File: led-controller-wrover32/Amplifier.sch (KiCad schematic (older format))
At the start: 5 parts, among them J11 Conn_01x02, U5 MAX98357A

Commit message: Cleanup
Signed-off-by: Aaron Williams <aaron.w2@gmail.com>
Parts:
- added J10: Conn_01x02 DNS, Connector_PinHeader_1.27mm:PinHeader_1x02_P1.27mm_Vertical_SMD_Pin1Left, symbol Connector_Generic:Conn_01x02
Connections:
- net SPKR+: now also J10.1 (Pin_1)
- net SPKR-: now also J10.2 (Pin_2)
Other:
- moved on the sheet: J11
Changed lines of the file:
@@
 EESchema Schematic File Version 4
-LIBS:led-controller-wrover32-cache
 EELAYER 30 0
 EELAYER END
 $Descr A4 11693 8268
 encoding utf-8
-Sheet 3 4
+Sheet 3 5
 Title ""
 Date ""
@@
 	1    0    0    -1
 $EndComp
-$Comp
-L Connector_Generic:Conn_01x02 J11
-U 1 1 5DBCE011
-P 5100 3200
-F 0 "J11" H 5180 3192 50  0000 L CNN
-F 1 "Conn_01x02" H 5180 3101 50  0000 L CNN
-F 2 "Aaron:JST_SH_BM02B-SRSS-TB_1x02-1MP_P1.00mm_Vertical" H 5100 3200 50  0001 C CNN
-F 3 "https://media.digikey.com/pdf/Data%20Sheets/JST%20PDFs/SR%20Connector.pdf" H 5100 3200 50  0001 C CNN
-F 4 "JST Sales America Inc." H 5100 3200 50  0001 C CNN "MFR"
-F 5 "BM02B-SRSS-TB(LF)(SN)" H 5100 3200 50  0001 C CNN "MPN"
-F 6 "Digikey" H 5100 3200 50  0001 C CNN "SPR"
-F 7 "455-1788-1-ND" H 5100 3200 50  0001 C CNN "SPN"
-F 8 "https://www.digikey.com/product-detail/en/jst-sales-america-inc/BM02B-SRSS-TB-LF-SN/455-1788-1-ND/926859" H 5100 3200 50  0001 C CNN "SPURL"
-	1    5100 3200
-	1    0    0    -1
-$EndComp
 Wire Wire Line
 	3200 3100 2650 3100
@@
 SPKR-
 Wire Wire Line
+	4550 3100 4900 3100
+Wire Wire Line
 	4900 3100 4900 3200
-Wire Wire Line
-	4550 3100 4900 3100
-Wire Wire Line
-	4550 3300 4900 3300
+$Comp
+L Connector_Generic:Conn_01x02 J11
+U 1 1 5DBCE011
+P 5200 3200
+F 0 "J11" H 5280 3192 50  0000 L CNN
+F 1 "Conn_01x02" H 5280 3101 50  0000 L CNN
+F 2 "Aaron:JST_SH_BM02B-SRSS-TB_1x02-1MP_P1.00mm_Vertical" H 5200 3200 50  0001 C CNN
+F 3 "https://media.digikey.com/pdf/Data%20Sheets/JST%20PDFs/SR%20Connector.pdf" H 5200 3200 50  0001 C CNN
+F 4 "JST Sales America Inc." H 5200 3200 50  0001 C CNN "MFR"
+F 5 "BM02B-SRSS-TB(LF)(SN)" H 5200 3200 50  0001 C CNN "MPN"
+F 6 "Digikey" H 5200 3200 50  0001 C CNN "SPR"
+F 7 "455-1788-1-ND" H 5200 3200 50  0001 C CNN "SPN"
+F 8 "https://www.digikey.com/product-detail/en/jst-sales-america-inc/BM02B-SRSS-TB-LF-SN/455-1788-1-ND/926859" H 5200 3200 50  0001 C CNN "SPURL"
+	1    5200 3200
+	1    0    0    -1
+$EndComp
+$Comp
+L Connector_Generic:Conn_01x02 J10
+U 1 1 5E133F76
+P 5200 3600
+F 0 "J10" H 5280 3592 50  0000 L CNN
+F 1 "Conn_01x02 DNS" H 5280 3501 50  0000 L CNN
+F 2 "Connector_PinHeader_1.27mm:PinHeader_1x02_P1.27mm_Vertical_SMD_Pin1Left" H 5200 3600 50  0001 C CNN
+F 3 "https://media.digikey.com/pdf/Data%20Sheets/JST%20PDFs/SR%20Connector.pdf" H 5200 3600 50  0001 C CNN
+F 4 "JST Sales America Inc." H 5200 3600 50  0001 C CNN "MFR"
+F 5 "BM02B-SRSS-TB(LF)(SN)" H 5200 3600 50  0001 C CNN "MPN"
+F 6 "Digikey" H 5200 3600 50  0001 C CNN "SPR"
+F 7 "455-1788-1-ND" H 5200 3600 50  0001 C CNN "SPN"
+F 8 "https://www.digikey.com/product-detail/en/jst-sales-america-inc/BM02B-SRSS-TB-LF-SN/455-1788-1-ND/926859" H 5200 3600 50  0001 C CNN "SPURL"
+	1    5200 3600
+	1    0    0    -1
+$EndComp
+Wire Wire Line
+	4900 3200 5000 3200
+Wire Wire Line
+	4550 3300 4800 3300
+Wire Wire Line
+	4900 3200 4900 3600
+Wire Wire Line
+	4900 3600 5000 3600
+Connection ~ 4900 3200
+Wire Wire Line
+	4800 3300 4800 3700
+Wire Wire Line
+	4800 3700 5000 3700
+Connection ~ 4800 3300
+Wire Wire Line
+	4800 3300 5000 3300
 $EndSCHEMATC

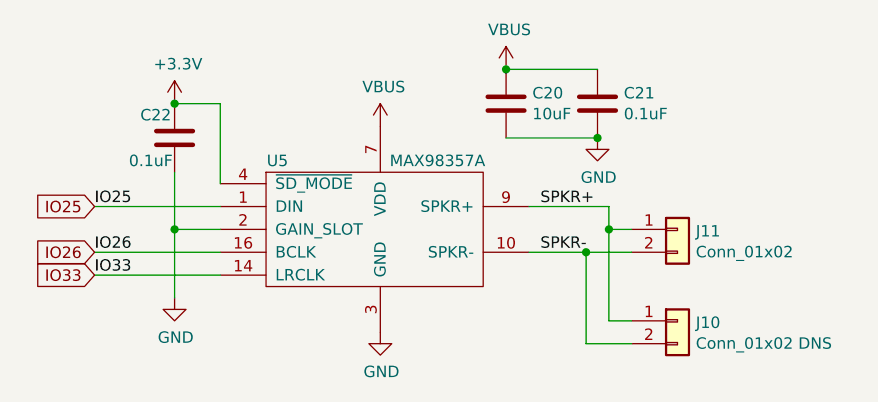
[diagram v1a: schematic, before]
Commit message: Fix reset circuit and other stuff
This fixes the reset circuit and moves a few components.  It also
cleans up the BOM a bit.

Also bumped to version 3.5.0

Signed-off-by: Aaron Williams <aaron.w2@gmail.com>
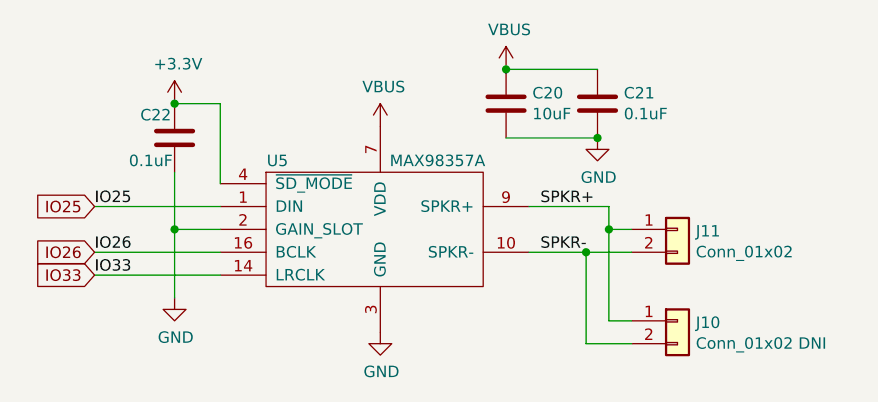
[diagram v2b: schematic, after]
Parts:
- C20, C21, C22: MFR (none) -> -; MPN (none) -> -; SPN (none) -> -; SPR (none) -> -; SPURL (none) -> -
- J10: value Conn_01x02 DNS -> Conn_01x02 DNI
